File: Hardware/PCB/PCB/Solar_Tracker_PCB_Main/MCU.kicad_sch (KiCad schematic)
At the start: 16 parts, among them IC1 ESP32-S3-WROOM-1-N4R8, IC5 LM1117MPX-3.3_NOPB, J2 USB4940-00-A, J3 1729076, J4 1977223-1, J5 1977223-1

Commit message: Bornera
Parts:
- added C22: 10u, Capacitor_SMD:C_0805_2012Metric_Pad1.18x1.45mm_HandSolder, symbol Device:C
- added R11, R19, R20: 10k, Resistor_SMD:R_0805_2012Metric_Pad1.20x1.40mm_HandSolder, symbol Device:R
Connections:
- net GND: now also J3.2, J3.4, J3.6, J3.8, C22.2
- net VDD: now also J3.1, C22.1, R11.1, R19.1, R20.1
- net SL_SCL: now reaches J3.3
- net SL_SCL: now also R11.2
- net SL_SDA: now reaches J3.5
- net SL_SDA: now also R19.2
- net SL_INT: now reaches J3.7
- net SL_INT: now also R20.2
- no-connect marks 36 -> 28
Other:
- moved on the sheet: J3

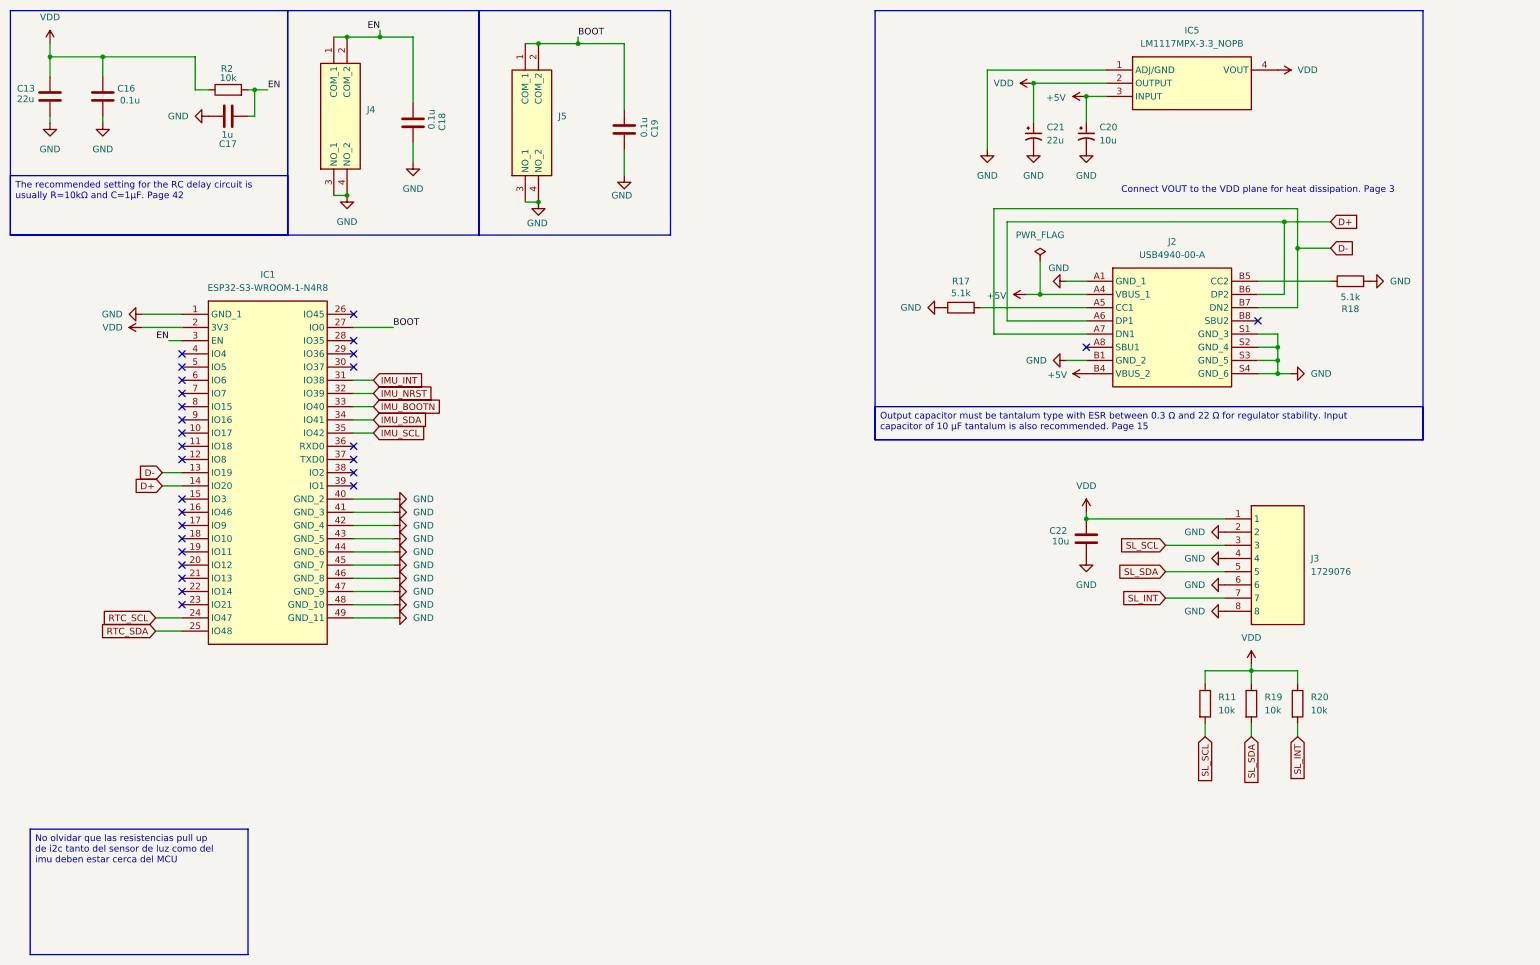
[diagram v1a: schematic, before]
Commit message: Calculo de resistencias PullUp para la placa Satelite
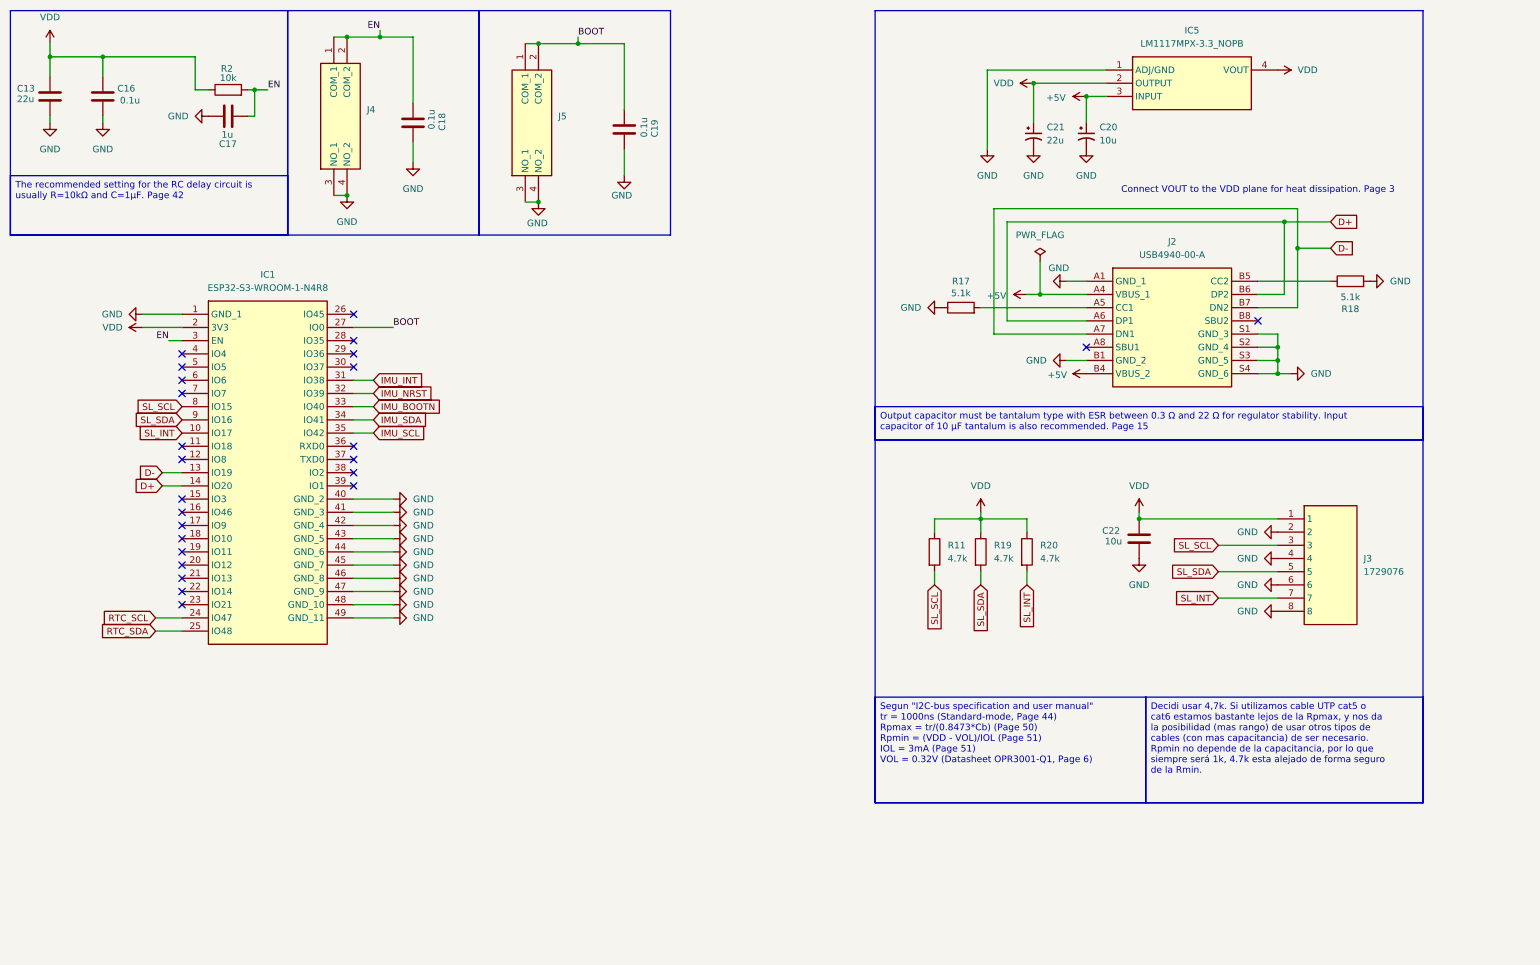
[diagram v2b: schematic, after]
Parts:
- R11, R19, R20: value 10k -> 4.7k
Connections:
- net SL_INT: now also IC1.10 (IO17)
- net SL_SCL: now also IC1.8 (IO15)
- net SL_SDA: now also IC1.9 (IO16)
- no-connect marks 28 -> 25
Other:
- moved on the sheet: C22, J3, R11, R19, R20

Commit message: comienzo de distribucion pcb
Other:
- moved on the sheet: C20, C21, IC1, IC5

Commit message: Colocacion de los componentes en el PCB
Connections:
- net RTC_SCL: now also IC1.25 (IO48); no longer IC1.24 (IO47)
- net RTC_SDA: now also IC1.24 (IO47); no longer IC1.25 (IO48)
